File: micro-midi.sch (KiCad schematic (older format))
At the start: 14 parts, among them J1 AudioJack3, J2 Conn_01x04_Male, J3 AudioJack3, U1 74HC04, U2 6N137

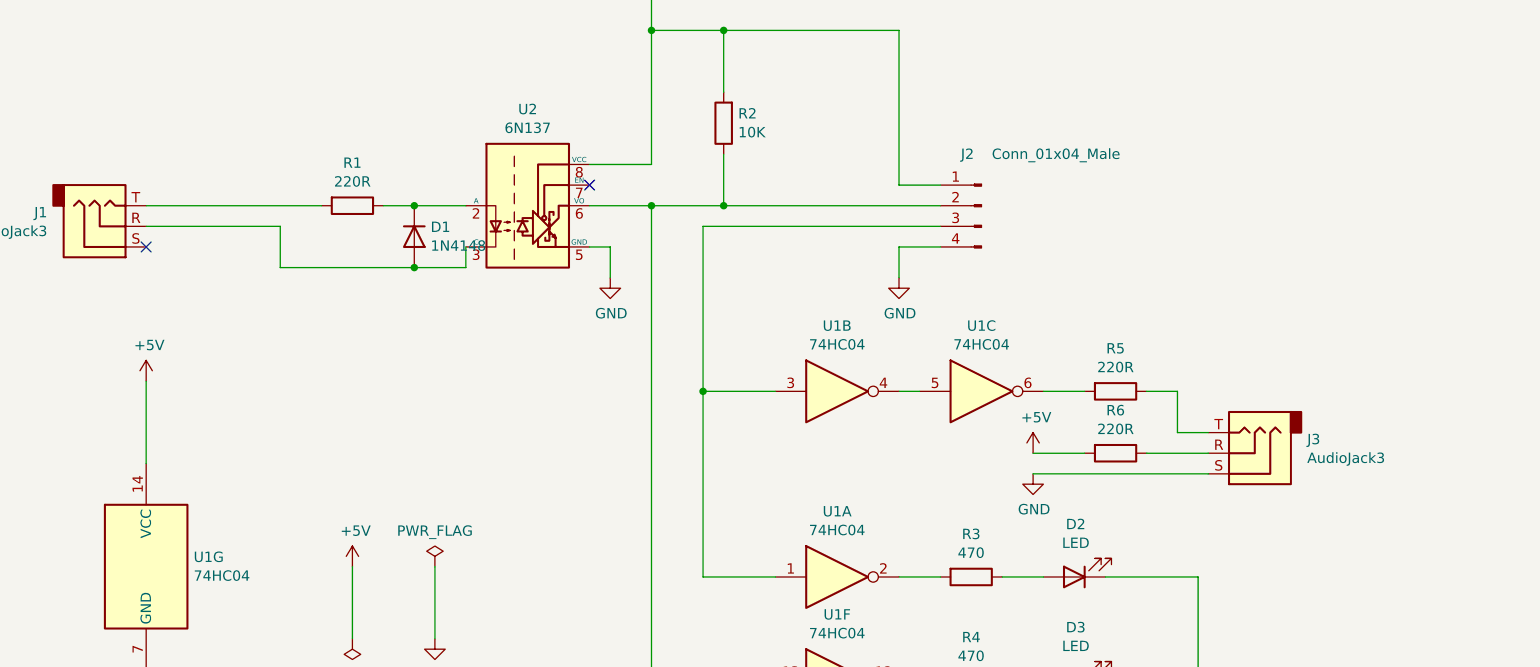
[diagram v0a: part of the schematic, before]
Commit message: add ferrites to schematic
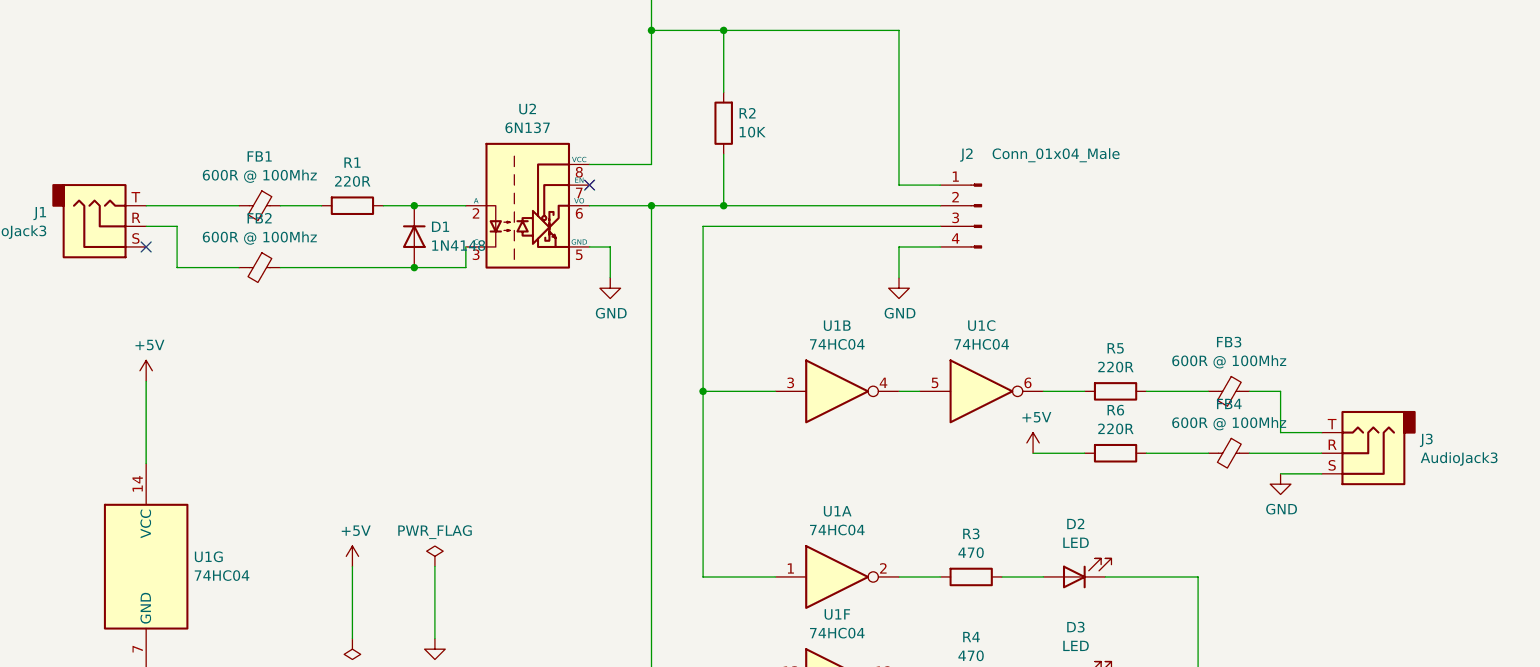
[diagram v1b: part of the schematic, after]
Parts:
- added FB1, FB2, FB3, FB4: 600R @ 100Mhz, Resistor_SMD:R_0805_2012Metric_Pad1.15x1.40mm_HandSolder, symbol Device:Ferrite_Bead_Small
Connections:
- net at D1.2 (A), U2.3 (C): now also FB2.1; no longer J1.R
- net at J1.T: now also FB1.2; no longer R1.2
- net at J3.R: now also FB4.1; no longer R6.1
- net at J3.T: now also FB3.1; no longer R5.1
- new net: FB2.2, J1.R
- new net: FB1.1, R1.2
- new net: FB3.2, R5.1
- new net: FB4.2, R6.1
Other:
- moved on the sheet: J3
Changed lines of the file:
@@
 Wire Wire Line
 	4450 3100 3800 3100
-Wire Wire Line
-	3800 3100 3800 2900
-Wire Wire Line
-	3800 2900 3150 2900
 Connection ~ 4450 3100
 NoConn ~ 5300 2700
@@
 Connection ~ 4450 2800
 Wire Wire Line
-	3150 2800 4000 2800
-Wire Wire Line
 	4300 2800 4450 2800
 $Comp
@@
 	0    1    1    0
 $EndComp
-Wire Wire Line
-	8150 3900 8300 3900
-Wire Wire Line
-	8000 3700 8150 3700
 $Comp
 L Device:R R5
@@
 L Connector:AudioJack3 J3
 U 1 1 5E8296E3
-P 8500 4000
-F 0 "J3" H 8221 3933 50  0000 R CNN
-F 1 "AudioJack3" H 8221 4024 50  0000 R CNN
-F 2 "Connector_Audio:Jack_3.5mm_QingPu_WQP-PJ398SM_Vertical_CircularHoles" H 8500 4000 50  0001 C CNN
-F 3 "~" H 8500 4000 50  0001 C CNN
-	1    8500 4000
+P 9050 4000
+F 0 "J3" H 8771 3933 50  0000 R CNN
+F 1 "AudioJack3" H 8771 4024 50  0000 R CNN
+F 2 "Connector_Audio:Jack_3.5mm_QingPu_WQP-PJ398SM_Vertical_CircularHoles" H 9050 4000 50  0001 C CNN
+F 3 "~" H 9050 4000 50  0001 C CNN
+	1    9050 4000
 	-1   0    0    1
 $EndComp
@@
 Wire Wire Line
 	5850 4600 6200 4600
-Wire Wire Line
-	8150 3700 8150 3900
-Wire Wire Line
-	7450 4100 8300 4100
 $Comp
 L power:GND #PWR010
 U 1 1 5EA4A4EF
-P 7450 4100
-F 0 "#PWR010" H 7450 3850 50  0001 C CNN
-F 1 "GND" H 7455 3927 50  0000 C CNN
-F 2 "" H 7450 4100 50  0001 C CNN
-F 3 "" H 7450 4100 50  0001 C CNN
-	1    7450 4100
+P 8650 4100
+F 0 "#PWR010" H 8650 3850 50  0001 C CNN
+F 1 "GND" H 8655 3927 50  0000 C CNN
+F 2 "" H 8650 4100 50  0001 C CNN
+F 3 "" H 8650 4100 50  0001 C CNN
+	1    8650 4100
 	1    0    0    -1
 $EndComp
@@
 Wire Wire Line
 	5850 3700 5850 4600
+$Comp
+L Device:Ferrite_Bead_Small FB1
+U 1 1 5EDC636E
+P 3700 2800
+F 0 "FB1" V 3463 2800 50  0000 C CNN
+F 1 "600R @ 100Mhz" V 3554 2800 50  0000 C CNN
+F 2 "Resistor_SMD:R_0805_2012Metric_Pad1.15x1.40mm_HandSolder" V 3630 2800 50  0001 C CNN
+F 3 "~" H 3700 2800 50  0001 C CNN
+	1    3700 2800
+	0    1    1    0
+$EndComp
+$Comp
+L Device:Ferrite_Bead_Small FB2
+U 1 1 5EDC7A59
+P 3700 3100
+F 0 "FB2" V 3463 3100 50  0000 C CNN
+F 1 "600R @ 100Mhz" V 3554 3100 50  0000 C CNN
+F 2 "Resistor_SMD:R_0805_2012Metric_Pad1.15x1.40mm_HandSolder" V 3630 3100 50  0001 C CNN
+F 3 "~" H 3700 3100 50  0001 C CNN
+	1    3700 3100
+	0    1    1    0
+$EndComp
+Wire Wire Line
+	3600 3100 3300 3100
+Wire Wire Line
+	3300 3100 3300 2900
+Wire Wire Line
+	3300 2900 3150 2900
+Wire Wire Line
+	3150 2800 3600 2800
+Wire Wire Line
+	3800 2800 4000 2800
+$Comp
+L Device:Ferrite_Bead_Small FB3
+U 1 1 5EDCC5FB
+P 8400 3700
+F 0 "FB3" V 8163 3700 50  0000 C CNN
+F 1 "600R @ 100Mhz" V 8254 3700 50  0000 C CNN
+F 2 "Resistor_SMD:R_0805_2012Metric_Pad1.15x1.40mm_HandSolder" V 8330 3700 50  0001 C CNN
+F 3 "~" H 8400 3700 50  0001 C CNN
+	1    8400 3700
+	0    1    1    0
+$EndComp
+$Comp
+L Device:Ferrite_Bead_Small FB4
+U 1 1 5EDCCBAB
+P 8400 4000
+F 0 "FB4" V 8163 4000 50  0000 C CNN
+F 1 "600R @ 100Mhz" V 8254 4000 50  0000 C CNN
+F 2 "Resistor_SMD:R_0805_2012Metric_Pad1.15x1.40mm_HandSolder" V 8330 4000 50  0001 C CNN
+F 3 "~" H 8400 4000 50  0001 C CNN
+	1    8400 4000
+	0    1    1    0
+$EndComp
+Wire Wire Line
+	8000 3700 8300 3700
+Wire Wire Line
+	8500 3700 8650 3700
+Wire Wire Line
+	8650 3700 8650 3900
+Wire Wire Line
+	8650 3900 8850 3900
+Wire Wire Line
+	8850 4000 8500 4000
+Wire Wire Line
+	8650 4100 8850 4100
 $EndSCHEMATC

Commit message: add some mouser part numbers
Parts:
- FB1, FB2, FB3, FB4: Mouser (none) -> 81-BLM21A601F
- R1, R5, R6: Mouser (none) -> 667-ERJ-6ENF2200V
- R2: Mouser (none) -> 667-ERJ-6ENF1002V
- R3, R4: value 470 -> 470R; Mouser (none) -> 667-ERJ-6ENF4700V
- U1: footprint (none) -> Package_SO:SOIC-14_3.9x8.7mm_P1.27mm
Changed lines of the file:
@@
 F 2 "Resistor_SMD:R_0805_2012Metric_Pad1.15x1.40mm_HandSolder" V 5880 2400 50  0001 C CNN
 F 3 "~" H 5950 2400 50  0001 C CNN
+F 4 " 667-ERJ-6ENF1002V " H 5950 2400 50  0001 C CNN "Mouser"
 	1    5950 2400
 	-1   0    0    1
@@
 F 0 "U1" H 2100 5267 50  0000 C CNN
 F 1 "74HC04" H 2100 5176 50  0000 C CNN
-F 2 "" H 2100 4950 50  0001 C CNN
+F 2 "Package_SO:SOIC-14_3.9x8.7mm_P1.27mm" H 2100 4950 50  0001 C CNN
 F 3 "https://assets.nexperia.com/documents/data-sheet/74HC_HCT04.pdf" H 2100 4950 50  0001 C CNN
 	4    2100 4950
@@
 P 7150 4600
 F 0 "R3" V 6943 4600 50  0000 C CNN
-F 1 "470" V 7034 4600 50  0000 C CNN
+F 1 "470R" V 7034 4600 50  0000 C CNN
 F 2 "Resistor_SMD:R_0805_2012Metric_Pad1.15x1.40mm_HandSolder" V 7080 4600 50  0001 C CNN
 F 3 "~" H 7150 4600 50  0001 C CNN
+F 4 "667-ERJ-6ENF4700V" H 7150 4600 50  0001 C CNN "Mouser"
 	1    7150 4600
 	0    1    1    0
@@
 P 7150 5100
 F 0 "R4" V 6943 5100 50  0000 C CNN
-F 1 "470" V 7034 5100 50  0000 C CNN
+F 1 "470R" V 7034 5100 50  0000 C CNN
 F 2 "Resistor_SMD:R_0805_2012Metric_Pad1.15x1.40mm_HandSolder" V 7080 5100 50  0001 C CNN
 F 3 "~" H 7150 5100 50  0001 C CNN
+F 4 "667-ERJ-6ENF4700V" H 7150 5100 50  0001 C CNN "Mouser"
 	1    7150 5100
 	0    1    1    0
@@
 F 0 "U1" H 2100 4567 50  0000 C CNN
 F 1 "74HC04" H 2100 4476 50  0000 C CNN
-F 2 "" H 2100 4250 50  0001 C CNN
+F 2 "Package_SO:SOIC-14_3.9x8.7mm_P1.27mm" H 2100 4250 50  0001 C CNN
 F 3 "https://assets.nexperia.com/documents/data-sheet/74HC_HCT04.pdf" H 2100 4250 50  0001 C CNN
 	5    2100 4250
@@
 F 0 "U1" H 6500 5417 50  0000 C CNN
 F 1 "74HC04" H 6500 5326 50  0000 C CNN
-F 2 "" H 6500 5100 50  0001 C CNN
+F 2 "Package_SO:SOIC-14_3.9x8.7mm_P1.27mm" H 6500 5100 50  0001 C CNN
 F 3 "https://assets.nexperia.com/documents/data-sheet/74HC_HCT04.pdf" H 6500 5100 50  0001 C CNN
 	6    6500 5100
@@
 F 0 "U1" H 3380 4596 50  0000 L CNN
 F 1 "74HC04" H 3380 4505 50  0000 L CNN
-F 2 "" H 3150 4550 50  0001 C CNN
+F 2 "Package_SO:SOIC-14_3.9x8.7mm_P1.27mm" H 3150 4550 50  0001 C CNN
 F 3 "https://assets.nexperia.com/documents/data-sheet/74HC_HCT04.pdf" H 3150 4550 50  0001 C CNN
 	7    3150 4550
@@
 F 2 "Resistor_SMD:R_0805_2012Metric_Pad1.15x1.40mm_HandSolder" V 4080 2800 50  0001 C CNN
 F 3 "~" H 4150 2800 50  0001 C CNN
+F 4 " 667-ERJ-6ENF2200V " H 4150 2800 50  0001 C CNN "Mouser"
 	1    4150 2800
 	0    1    1    0
@@
 F 2 "Resistor_SMD:R_0805_2012Metric_Pad1.15x1.40mm_HandSolder" V 7780 4000 50  0001 C CNN
 F 3 "~" H 7850 4000 50  0001 C CNN
+F 4 " 667-ERJ-6ENF2200V " H 7850 4000 50  0001 C CNN "Mouser"
 	1    7850 4000
 	0    1    1    0
@@
 F 2 "Resistor_SMD:R_0805_2012Metric_Pad1.15x1.40mm_HandSolder" V 7780 3700 50  0001 C CNN
 F 3 "~" H 7850 3700 50  0001 C CNN
+F 4 " 667-ERJ-6ENF2200V " H 7850 3700 50  0001 C CNN "Mouser"
 	1    7850 3700
 	0    1    1    0
@@
 F 0 "U1" H 6500 4017 50  0000 C CNN
 F 1 "74HC04" H 6500 3926 50  0000 C CNN
-F 2 "" H 6500 3700 50  0001 C CNN
+F 2 "Package_SO:SOIC-14_3.9x8.7mm_P1.27mm" H 6500 3700 50  0001 C CNN
 F 3 "https://assets.nexperia.com/documents/data-sheet/74HC_HCT04.pdf" H 6500 3700 50  0001 C CNN
 	2    6500 3700
@@
 F 0 "U1" H 7200 4017 50  0000 C CNN
 F 1 "74HC04" H 7200 3926 50  0000 C CNN
-F 2 "" H 7200 3700 50  0001 C CNN
+F 2 "Package_SO:SOIC-14_3.9x8.7mm_P1.27mm" H 7200 3700 50  0001 C CNN
 F 3 "https://assets.nexperia.com/documents/data-sheet/74HC_HCT04.pdf" H 7200 3700 50  0001 C CNN
 	3    7200 3700
@@
 F 2 "Resistor_SMD:R_0805_2012Metric_Pad1.15x1.40mm_HandSolder" V 3630 2800 50  0001 C CNN
 F 3 "~" H 3700 2800 50  0001 C CNN
+F 4 "81-BLM21A601F" H 3700 2800 50  0001 C CNN "Mouser"
 	1    3700 2800
 	0    1    1    0
@@
 F 2 "Resistor_SMD:R_0805_2012Metric_Pad1.15x1.40mm_HandSolder" V 3630 3100 50  0001 C CNN
 F 3 "~" H 3700 3100 50  0001 C CNN
+F 4 "81-BLM21A601F" H 3700 3100 50  0001 C CNN "Mouser"
 	1    3700 3100
 	0    1    1    0
@@
 F 2 "Resistor_SMD:R_0805_2012Metric_Pad1.15x1.40mm_HandSolder" V 8330 3700 50  0001 C CNN
 F 3 "~" H 8400 3700 50  0001 C CNN
+F 4 "81-BLM21A601F" V 8400 3700 50  0001 C CNN "Mouser"
 	1    8400 3700
 	0    1    1    0
@@
 F 2 "Resistor_SMD:R_0805_2012Metric_Pad1.15x1.40mm_HandSolder" V 8330 4000 50  0001 C CNN
 F 3 "~" H 8400 4000 50  0001 C CNN
+F 4 "81-BLM21A601F" H 8400 4000 50  0001 C CNN "Mouser"
 	1    8400 4000
 	0    1    1    0

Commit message: fix misconnected input
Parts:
- removed R2: 10K, Resistor_SMD:R_0805_2012Metric_Pad1.15x1.40mm_HandSolder, symbol Device:R
- added R2: 10k, Resistor_SMD:R_0805_2012Metric_Pad1.15x1.40mm_HandSolder, symbol Device:R_Small
- R1, R3, R4, R5, R6: symbol Device:R -> Device:R_Small
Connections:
- net +5V: now also R2.1
- net at J1.R: now also FB1.2; no longer FB2.2
- net at J1.T: now also FB2.2; no longer FB1.2
- net Tx: now reaches J2.2 (Pin_2), U1.13, U2.6 (VO)
- net Tx: now also R2.2
- net Rx: now reaches J2.3 (Pin_3), U1.1, U1.3
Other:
- moved on the sheet: J1
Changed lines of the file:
@@
 L Connector:AudioJack3 J1
 U 1 1 5E7D1AF1
-P 2950 2900
-F 0 "J1" H 2671 2833 50  0000 R CNN
-F 1 "AudioJack3" H 2671 2924 50  0000 R CNN
-F 2 "Connector_Audio:Jack_3.5mm_QingPu_WQP-PJ398SM_Vertical_CircularHoles" H 2950 2900 50  0001 C CNN
-F 3 "~" H 2950 2900 50  0001 C CNN
-	1    2950 2900
-	1    0    0    1
-$EndComp
-$Comp
-L Device:R R2
-U 1 1 5E7D2F1C
-P 5950 2400
-F 0 "R2" H 5880 2354 50  0000 R CNN
-F 1 "10K" H 5880 2445 50  0000 R CNN
-F 2 "Resistor_SMD:R_0805_2012Metric_Pad1.15x1.40mm_HandSolder" V 5880 2400 50  0001 C CNN
-F 3 "~" H 5950 2400 50  0001 C CNN
-F 4 " 667-ERJ-6ENF1002V " H 5950 2400 50  0001 C CNN "Mouser"
-	1    5950 2400
-	-1   0    0    1
+P 2950 3000
+F 0 "J1" H 2671 2933 50  0000 R CNN
+F 1 "AudioJack3" H 2671 3024 50  0000 R CNN
+F 2 "Connector_Audio:Jack_3.5mm_QingPu_WQP-PJ398SM_Vertical_CircularHoles" H 2950 3000 50  0001 C CNN
+F 3 "~" H 2950 3000 50  0001 C CNN
+	1    2950 3000
+	1    0    0    -1
 $EndComp
 $Comp
@@
 	1    0    0    -1
 $EndComp
-Wire Wire Line
-	5600 1150 5600 1950
-Wire Wire Line
-	5600 2600 5300 2600
-Connection ~ 5600 1950
-Wire Wire Line
-	5600 1950 5600 2600
-Wire Wire Line
-	5300 2800 5600 2800
-Wire Wire Line
-	5950 2250 5950 1950
-Connection ~ 5950 1950
-Wire Wire Line
-	5950 1950 5600 1950
-Wire Wire Line
-	5950 2550 5950 2800
 $Comp
 L Diode:1N4148 D1
@@
 Connection ~ 4450 3100
 NoConn ~ 5300 2700
-NoConn ~ 3150 3000
-Wire Wire Line
-	6800 2700 6800 1950
+NoConn ~ 3150 2900
 $Comp
 L Connector:Conn_01x04_Male J2
@@
 Wire Wire Line
 	6800 2700 7000 2700
-Wire Wire Line
-	5950 2800 7000 2800
-Connection ~ 5950 2800
-Wire Wire Line
-	7000 2900 5850 2900
 $Comp
 L 74xx:74HC04 U1
@@
 	5300 3000 5400 3000
 $Comp
-L Device:R R3
+L Device:R_Small R3
 U 1 1 5E84BB38
 P 7150 4600
@@
 $EndComp
 $Comp
-L Device:R R4
+L Device:R_Small R4
 U 1 1 5E84CE4D
 P 7150 5100
@@
 	-1   0    0    1
 $EndComp
-Wire Wire Line
-	6800 4600 7000 4600
-Wire Wire Line
-	7300 4600 7500 4600
-Wire Wire Line
-	6800 5100 7000 5100
-Wire Wire Line
-	7300 5100 7500 5100
 $Comp
 L 74xx:74HC04 U1
@@
 $EndComp
 Connection ~ 4450 2800
-Wire Wire Line
-	4300 2800 4450 2800
-$Comp
-L Device:R R1
+$Comp
+L Device:R_Small R1
 U 1 1 5E7D6E0A
 P 4150 2800
@@
 L power:+5V #PWR07
 U 1 1 5E7D8E69
-P 5600 1150
-F 0 "#PWR07" H 5600 1000 50  0001 C CNN
-F 1 "+5V" H 5615 1323 50  0000 C CNN
-F 2 "" H 5600 1150 50  0001 C CNN
-F 3 "" H 5600 1150 50  0001 C CNN
-	1    5600 1150
+P 6800 2550
+F 0 "#PWR07" H 6800 2400 50  0001 C CNN
+F 1 "+5V" H 6815 2723 50  0000 C CNN
+F 2 "" H 6800 2550 50  0001 C CNN
+F 3 "" H 6800 2550 50  0001 C CNN
+	1    6800 2550
 	1    0    0    -1
 $EndComp
@@
 $EndComp
 Wire Wire Line
-	5950 1950 6800 1950
-Wire Wire Line
 	4550 4550 4550 4900
 Wire Wire Line
@@
 	6800 3000 6800 3150
 Connection ~ 5600 2800
-Wire Wire Line
-	5600 2800 5950 2800
 $Comp
 L 74xx:74HC04 U1
@@
 	1    0    0    -1
 $EndComp
-Wire Wire Line
-	7450 4000 7700 4000
 $Comp
 L power:+5V #PWR09
@@
 	1    0    0    -1
 $EndComp
-Wire Wire Line
-	8000 4000 8300 4000
-$Comp
-L Device:R R6
+$Comp
+L Device:R_Small R6
 U 1 1 5EA76B1A
 P 7850 4000
@@
 $EndComp
 $Comp
-L Device:R R5
+L Device:R_Small R5
 U 1 1 5EA652C0
 P 7850 3700
@@
 	0    1    1    0
 $EndComp
-Wire Wire Line
-	7500 3700 7700 3700
 $Comp
 L Connector:AudioJack3 J3
@@
 	0    1    1    0
 $EndComp
-Wire Wire Line
-	3600 3100 3300 3100
-Wire Wire Line
-	3300 3100 3300 2900
-Wire Wire Line
-	3300 2900 3150 2900
-Wire Wire Line
-	3150 2800 3600 2800
-Wire Wire Line
-	3800 2800 4000 2800
 $Comp
 L Device:Ferrite_Bead_Small FB3
@@
 $EndComp
 Wire Wire Line
-	8000 3700 8300 3700
-Wire Wire Line
 	8500 3700 8650 3700
 Wire Wire Line
@@
 Wire Wire Line
 	8650 4100 8850 4100
+Wire Wire Line
+	3150 3100 3600 3100
+Wire Wire Line
+	3600 2800 3400 2800
+Wire Wire Line
+	3400 2800 3400 3000
+Wire Wire Line
+	3400 3000 3150 3000
+$Comp
+L Device:R_Small R2
+U 1 1 5EDDAA06
+P 5600 2700
+F 0 "R2" H 5659 2746 50  0000 L CNN
+F 1 "10k" H 5659 2655 50  0000 L CNN
+F 2 "Resistor_SMD:R_0805_2012Metric_Pad1.15x1.40mm_HandSolder" H 5600 2700 50  0001 C CNN
+F 3 "~" H 5600 2700 50  0001 C CNN
+F 4 " 667-ERJ-6ENF1002V " H 5600 2700 50  0001 C CNN "Mouser"
+	1    5600 2700
+	1    0    0    -1
+$EndComp
+Wire Wire Line
+	5300 2600 5600 2600
+Wire Wire Line
+	5300 2800 5600 2800
+Wire Wire Line
+	6800 2550 6800 2700
+$Comp
+L power:+5V #PWR?
+U 1 1 5EDDD8F7
+P 5600 2400
+F 0 "#PWR?" H 5600 2250 50  0001 C CNN
+F 1 "+5V" H 5615 2573 50  0000 C CNN
+F 2 "" H 5600 2400 50  0001 C CNN
+F 3 "" H 5600 2400 50  0001 C CNN
+	1    5600 2400
+	1    0    0    -1
+$EndComp
+Wire Wire Line
+	5600 2400 5600 2600
+Connection ~ 5600 2600
+Wire Wire Line
+	3800 2800 4050 2800
+Wire Wire Line
+	4250 2800 4450 2800
+Wire Wire Line
+	6800 5100 7050 5100
+Wire Wire Line
+	7250 5100 7500 5100
+Wire Wire Line
+	7250 4600 7500 4600
+Wire Wire Line
+	6800 4600 7050 4600
+Wire Wire Line
+	7500 3700 7750 3700
+Wire Wire Line
+	7450 4000 7750 4000
+Wire Wire Line
+	7950 4000 8300 4000
+Wire Wire Line
+	7950 3700 8300 3700
+Text Label 7000 2800 2    50   ~ 0
+Tx
+Text Label 5950 2800 2    50   ~ 0
+Tx
+Wire Wire Line
+	5600 2800 5950 2800
+Wire Wire Line
+	5850 2900 5950 2900
+Text Label 7000 2900 2    50   ~ 0
+Rx
+Text Label 5950 2900 2    50   ~ 0
+Rx
 $EndSCHEMATC
